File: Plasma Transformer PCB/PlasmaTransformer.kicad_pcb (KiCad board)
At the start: 2 copper layers, 90 x 90 mm, 92 parts, among them J1 Barrel_Jack_MountingPin, J10 Conn_01x01_Socket, J11 Screw_Terminal_01x01, J12 Screw_Terminal_01x01, J13 Conn_01x01_Socket, J14 Conn_01x01_Socket, J15 Conn_01x01_Socket, J16 Conn_01x01_Socket, J17 Conn_01x01_Socket, J18 Conn_01x01_Socket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

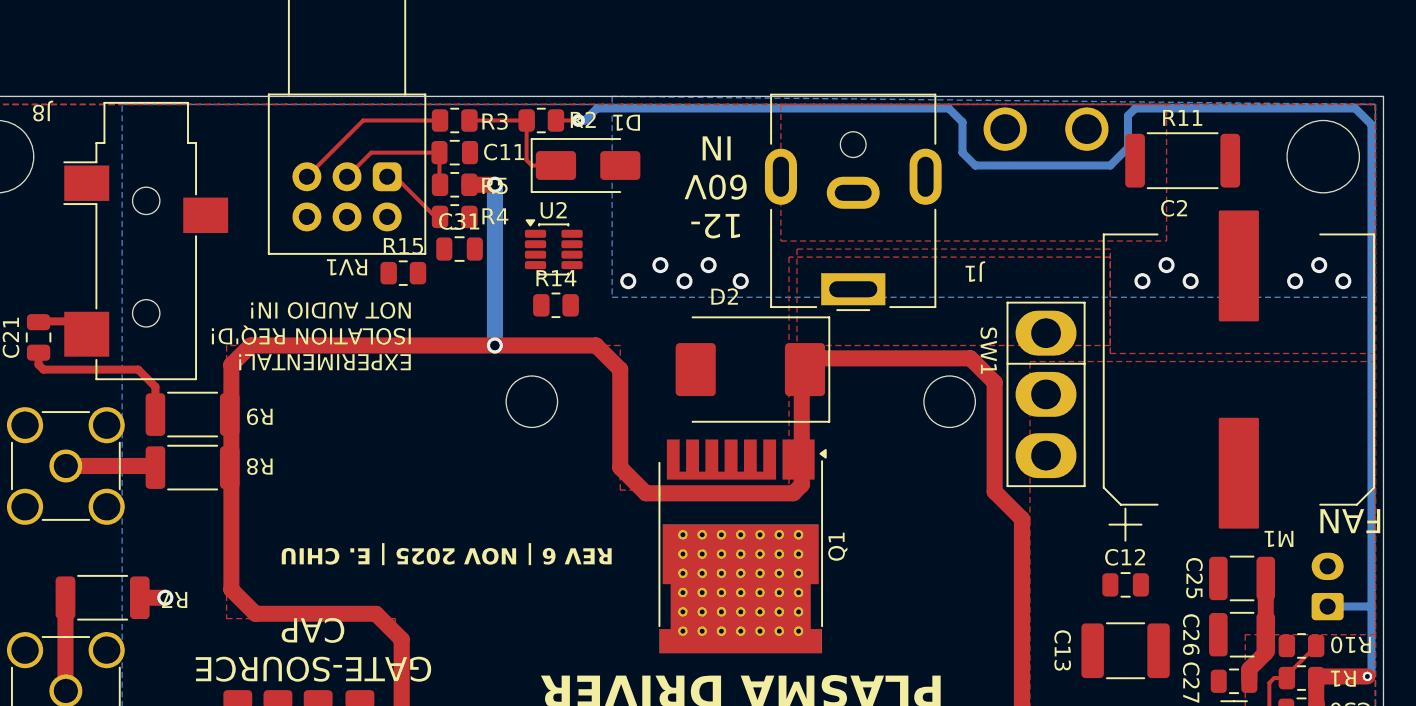
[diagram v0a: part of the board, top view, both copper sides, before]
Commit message: layout of feedback circuit
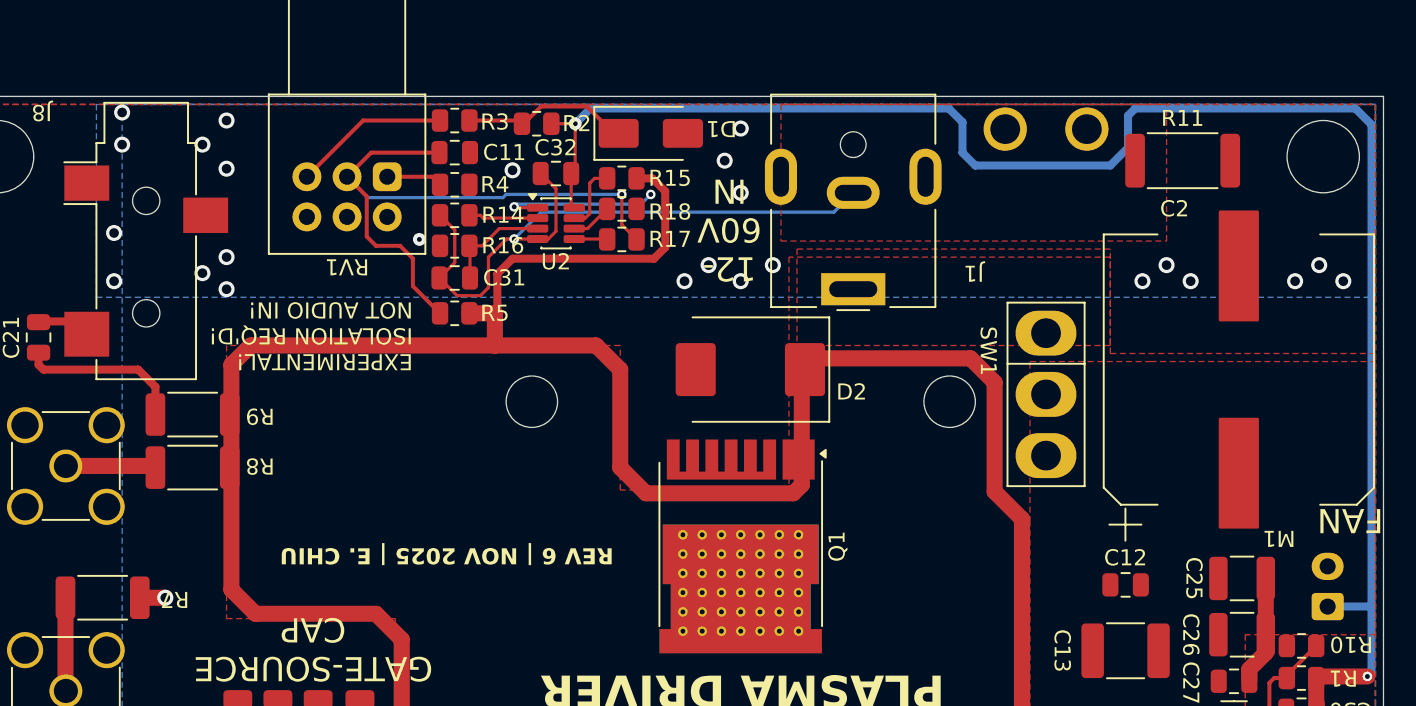
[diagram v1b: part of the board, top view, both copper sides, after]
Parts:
- added C32: 1nF, Capacitor_SMD:C_0805_2012Metric, F.Cu at (93.5, 59.8)
- added R16: 1k, Resistor_SMD:R_0805_2012Metric, F.Cu at (87.2, 64.3)
- added R17: 1k, Resistor_SMD:R_0805_2012Metric, F.Cu at (97.6, 63.9)
- added R18: 1k, Resistor_SMD:R_0805_2012Metric, F.Cu at (97.6, 62.0)
- U2: value LM358 -> TLV9302IDDFR
- moved R15 14.8 mm to (97.6, 60.1)
- moved R14 8.43 mm to (87.2, 62.4)
- moved R5 8.00 mm to (87.2, 68.5)
- moved D1 4.38 mm to (99.4, 57.3)
- moved R4 2.00 mm to (87.2, 60.5)
- moved C31 1.82 mm to (87.2, 66.3)
- moved U2 1.63 mm to (93.5, 62.9)
- moved R2 0.35 mm to (92.3, 56.7)
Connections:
- C31 pad 1: GND -> /GND-IN
- R14 pad 2: Net-(U2A-+) -> Net-(U2A--)
- U2 pad 1: Net-(U2B--) -> Net-(R12-Pad2)
- U2 pad 2: GND -> Net-(U2A--)
- U2 pad 4: GND -> /GND-IN
- U2 pad 5: unconnected-(U2B-+-Pad5) -> Net-(U2B-+)
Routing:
- net /GND-IN: track 0.00 -> 41.4 mm, vias 0 -> 1
- net Net-(C11-Pad2): track 8.39 -> 39.0 mm, vias 0 -> 1
- net /GATE: track 150.9 -> 162.1 mm, vias 2 -> 0
- net Net-(R12-Pad2): track 0.00 -> 10.3 mm, vias 0 -> 2
- net Net-(U2A-+): track 0.00 -> 6.71 mm
- net +12V: track 107.3 -> 112.8 mm
- net Net-(U2A--): track 0.00 -> 4.32 mm
- net Net-(R15-Pad1): track 0.00 -> 4.19 mm
- net Net-(U2B--): track 0.00 -> 2.56 mm
- net /REF10V: track 8.00 -> 10.4 mm
- net Net-(U2B-+): track 0.00 -> 2.06 mm
- net Net-(R4-Pad1): track 4.32 -> 3.78 mm
- net GND: vias 12 -> 26

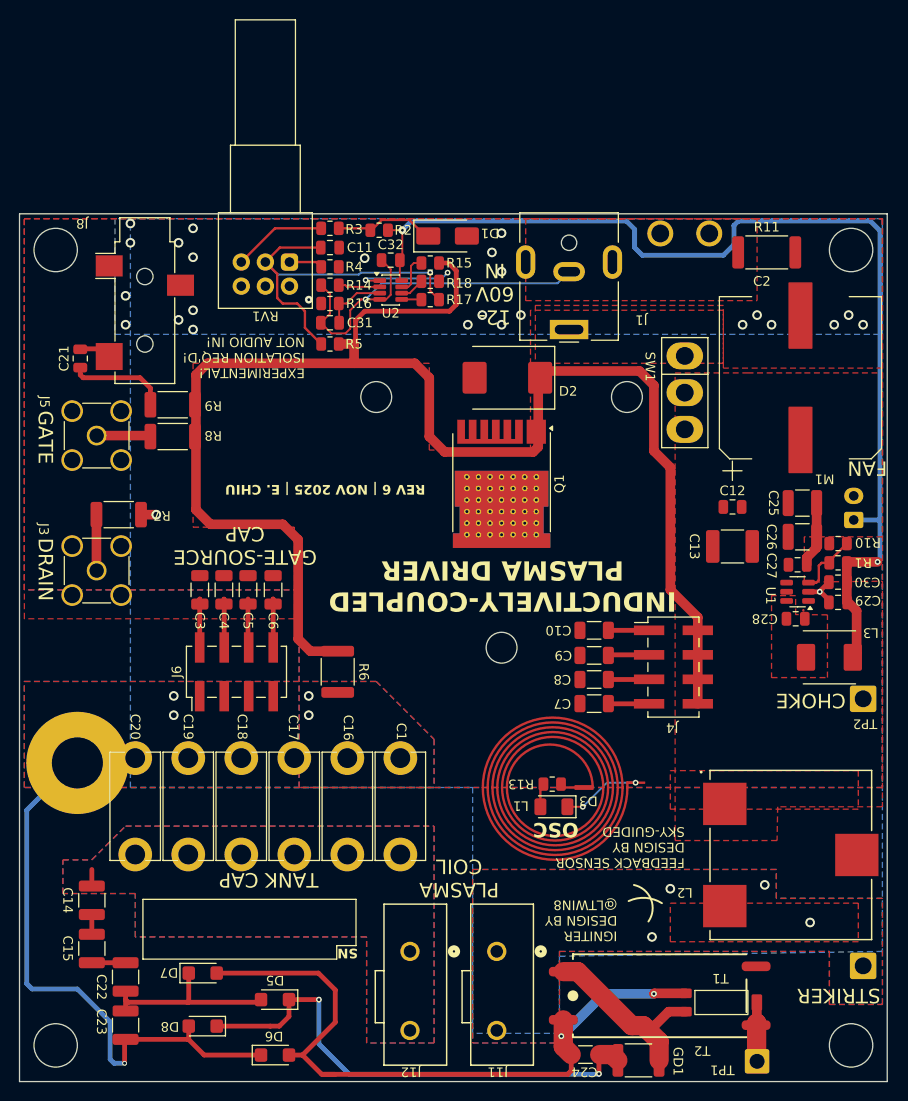
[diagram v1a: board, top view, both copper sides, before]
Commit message: routing complete, DRC check OK
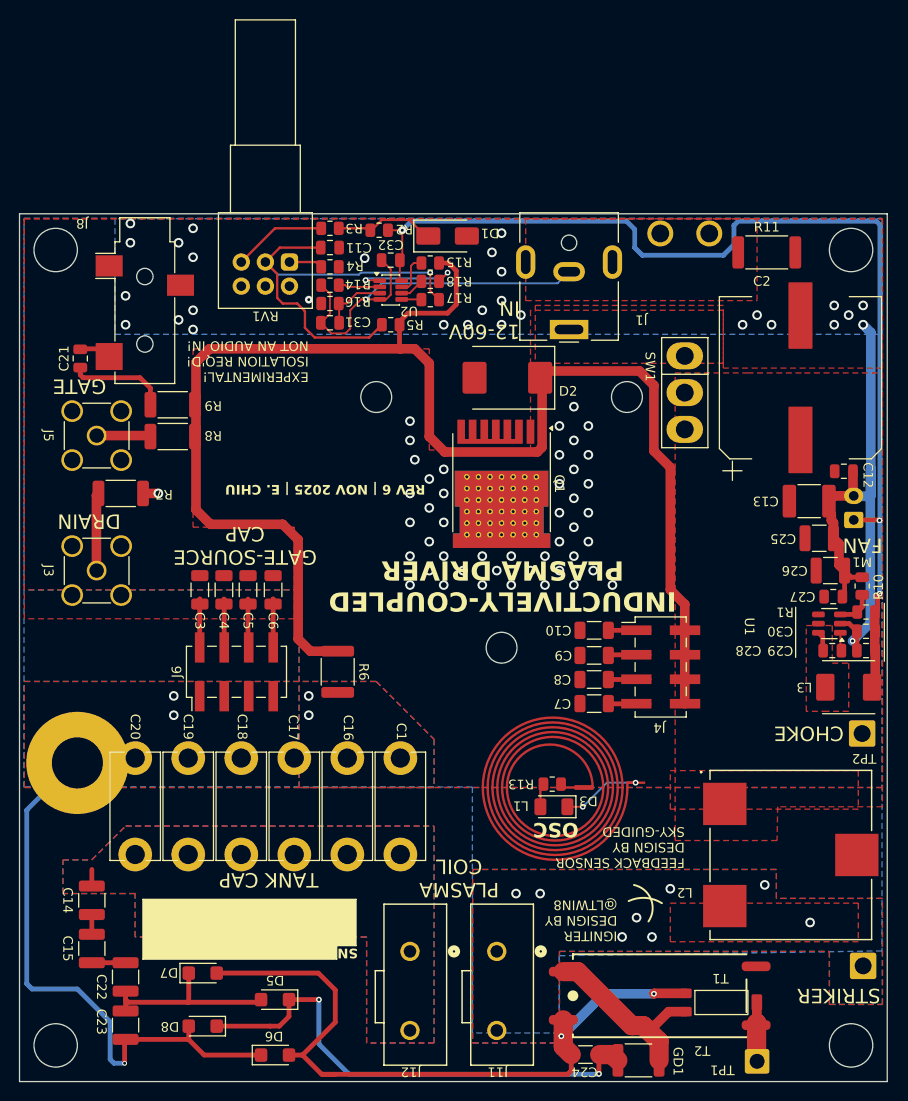
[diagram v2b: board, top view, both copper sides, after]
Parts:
- moved C12 12.1 mm to (140.5, 81.7), turned to 180 degrees
- moved C13 9.24 mm to (136.9, 84.8), turned to 180 degrees
- moved R5 6.61 mm to (93.5, 66.5)
- moved C30 5.87 mm to (142.8, 98.3)
- moved R1 5.87 mm to (142.8, 96.3)
- moved C29 5.78 mm to (142.8, 100.3)
- moved R10 5.06 mm to (142.4, 93.6), turned to 90 degrees
- moved C28 5.03 mm to (139.3, 100.3)
- moved C27 4.96 mm to (139.4, 94.7)
- moved U1 4.67 mm to (139.0, 97.5)
- moved C26 4.55 mm to (139.1, 92.0)
- moved C25 4.05 mm to (137.9, 88.7)
- moved L3 3.69 mm to (141.0, 104.1)
- moved TP2 3.60 mm to (142.4, 108.9)
- moved R7 2.21 mm to (65.5, 84.0)
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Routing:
- net GND: track 10.7 -> 63.6 mm, vias 26 -> 30
- net Net-(C11-Pad2): track 39.0 -> 45.6 mm
- net /GATE: track 162.1 -> 157.4 mm
- net Net-(U1-FB): track 6.63 -> 3.97 mm
- net Net-(J3-In): track 5.81 -> 8.10 mm
- net /12VSW: track 0.00 -> 2.05 mm
- net Net-(R12-Pad2): track 10.3 -> 11.6 mm
- net Net-(U1-CB): track 0.73 -> 1.90 mm
- net +12V: track 112.8 -> 113.0 mm, vias 2 -> 3
- net /DRAIN: vias 5 -> 54
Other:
- board text added: "12-60V IN"
- board text added: "EXPERIMENTAL! ISOLATION REQ'D! NOT AN AUDIO IN!"
- board text removed: "12- 60V IN"
- board text removed: "EXPERIMENTAL! ISOLATION REQ'D! NOT AUDIO IN!"

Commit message: add QR code for docs to backside silkscreen
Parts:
- added G***: LOGO, ALibrary:PlasmaTransformer-GitHub-QR-silk, B.Cu at (127.5, 133.5)
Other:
- board text added: "Plasma Transformer Documentation on GitHub Parts list, 3D prints, instructions, debugging"

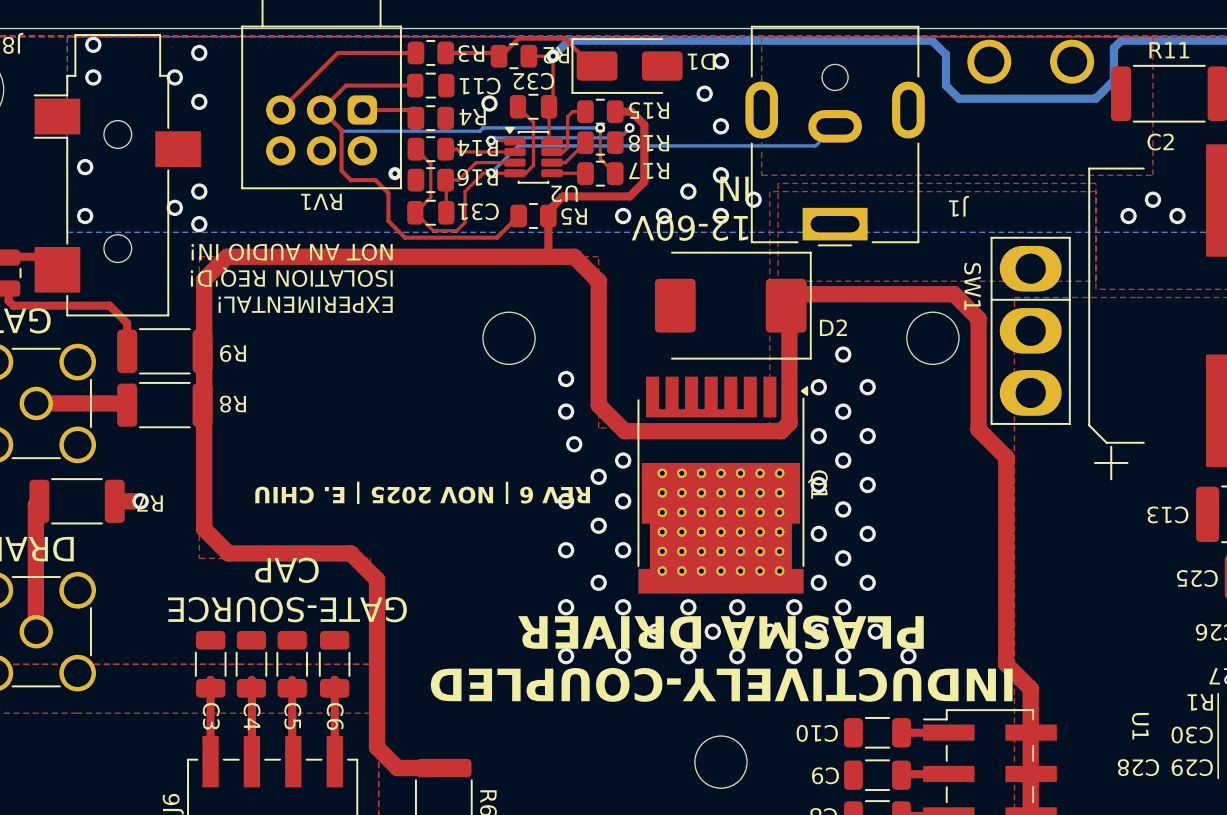
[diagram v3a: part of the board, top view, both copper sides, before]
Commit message: update silkscreens
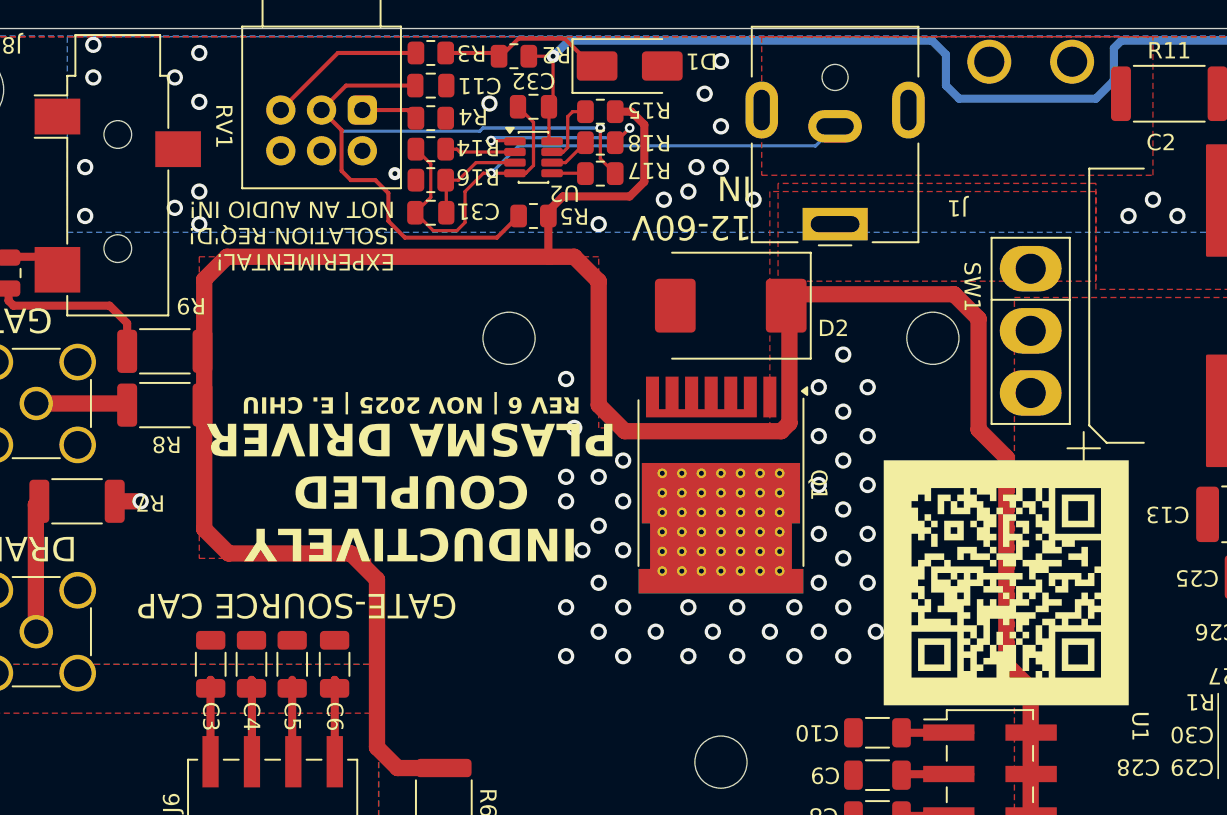
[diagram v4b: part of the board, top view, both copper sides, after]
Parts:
- added G***: LOGO, ALibrary:PlasmaTransformer-GitHub-QR-silk, F.Cu at (122.5, 89.0)
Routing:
- net /DRAIN: vias 54 -> 53
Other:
- board text added: "INDUCTIVELY COUPLED PLASMA DRIVER"
- board text removed: "INDUCTIVELY-COUPLED PLASMA DRIVER"

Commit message: generate manufacturing files
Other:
- board text added: "FAB NOTES: 1. FINISH: HASL LEAD FREE, ALTERNATE ENIG OK 2. SOLDERMASK: BLACK 3. SILKSCREEN: WHITE 4. LAYERS: 2 5. TOP AND BOTTOM WEIGHT: 1OZ 6. INNER LAYERS WEIGHT: 1OZ 7. TRACE/SPACE: 6MIL/6MIL 8. MINIMUM DRILL: 0.3MM 9. FINISHED THICKNESS: 1.6MM 10: CONTROLLED IMPEDANCE: NO 11. ITAR: NO 12. BOARD DIMENSIONS: 90MM x 90MM ASSY NOTES: 1. CLASS 2 ASSEMBLY 2. LEAD-FREE SOLDER 3. DO NOT POPULATE REFE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"
- board text added: "GATE-DRAIN CAP"
- board text removed: "FAB NOTES: 1. FINISH: HASL LEAD FREE, ALTERNATE ENIG OK 2. SOLDERMASK: WHITE 3. SILKSCREEN: BLACK 4. LAYERS: 2 5. TOP AND BOTTOM WEIGHT: 1OZ 6. INNER LAYERS WEIGHT: 1OZ 7. TRACE/SPACE: 6MIL/6MIL 8. MINIMUM DRILL: 0.3MM 9. FINISHED THICKNESS: 1.6MM 10: CONTROLLED IMPEDANCE: NO 11. ITAR: NO 12. BOARD DIMENSIONS: 90MM x 90MM ASSY NOTES: 1. CLASS 2 ASSEMBLY 2. LEAD-FREE SOLDER 3. DO NOT POPULATE REFE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"
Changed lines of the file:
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@@
 		(tenting front back)
 		(pcbplotparams
-			(layerselection 0x00000000_00000000_55555f55_575775ff)
+			(layerselection 0x00000000_00000000_55555f5d_575775ff)
 			(plot_on_all_layers_selection 0x00000000_00000000_00000000_00000000)
 			(disableapertmacros no)
@@
 		(tags "resistor")
 		(property "Reference" "R11"
-			(at 0 -2.63 0)
+			(at 0 -2.7 180)
 			(unlocked yes)
 			(layer "F.SilkS")
@@
 		(tags "Diode SMC (DO-214AB)")
 		(property "Reference" "D2"
-			(at -6.3 -1.4 0)
+			(at -6.3 -1.2 180)
 			(unlocked yes)
 			(layer "F.SilkS")
@@
 		(tags "Surface mounted pin header SMD 2x04 2.54mm double row")
 		(property "Reference" "J4"
-			(at -0.125 6.29 180)
+			(at 5.7 3.9 180)
 			(unlocked yes)
 			(layer "F.SilkS")
@@
 		(tags "capacitor electrolytic")
 		(property "Reference" "C2"
-			(at 10 -4 0)
+			(at 9.4 -7.6 180)
 			(unlocked yes)
 			(layer "F.SilkS")
@@
 		(tags "resistor")
 		(property "Reference" "R10"
-			(at -0.1 1.7 90)
+			(at 0.3 1.6 270)
 			(unlocked yes)
 			(layer "F.SilkS")
@@
 		(layer "User.2")
 	)
+	(gr_rect
+		(start 59.4 88.6)
+		(end 66.4 96)
+		(stroke
+			(width 0.1)
+			(type solid)
+		)
+		(fill yes)
+		(layer "User.2")
+	)
 	(gr_circle
 		(center 60.9 111.8)
@@
 	)
 	(gr_rect
-		(start 77.25 32.4)
-		(end 89.75 54.9)
+		(start 74.15 33.15)
+		(end 86.65 55.65)
 		(stroke
 			(width 0.1)
@@
 	)
 	(gr_rect
-		(start 174.5 121.5)
-		(end 181.5 133.5)
+		(start 118.1 95.9)
+		(end 125.1 107.9)
 		(stroke
 			(width 0.1)
@@
 		(layer "User.2")
 	)
+	(gr_rect
+		(start 59.7 73.75)
+		(end 66.7 81.45)
+		(stroke
+			(width 0.1)
+			(type solid)
+		)
+		(fill yes)
+		(layer "User.2")
+	)
 	(gr_circle
 		(center 83.497056 121.5)
@@
 	)
 	(gr_rect
-		(start 130.25 41)
-		(end 142.75 46.5)
+		(start 105.85 51.8)
+		(end 118.35 57.3)
 		(stroke
 			(width 0.1)
@@
 		(layer "User.3")
 	)
+	(gr_rect
+		(start 82.334418 63.834418)
+		(end 131.795172 108.6)
+		(stroke
+			(width 0.1)
+			(type solid)
+		)
+		(fill yes)
+		(layer "User.3")
+	)
 	(gr_text "EXPERIMENTAL!\nISOLATION REQ'D!\nNOT AN AUDIO IN!"
 		(at 85 65.5 180)
@@
 		)
 	)
+	(gr_text "GATE-DRAIN CAP"
+		(at 116.8 107.8 180)
+		(layer "F.SilkS")
+		(effects
+			(font
+				(size 1.5 1.5)
+				(thickness 0.25)
+			)
+			(justify bottom)
+		)
+	)
 	(gr_text "REV 6 | NOV 2025 | E. CHIU"
 		(at 86 77.5 180)
@@
 		)
 	)
-	(gr_text "FAB NOTES:\n1. FINISH: HASL LEAD FREE, ALTERNATE ENIG OK\n2. SOLDERMASK: WHITE\n3. SILKSCREEN: BLACK\n4. LAYERS: 2\n5. TOP AND BOTTOM WEIGHT: 1OZ\n6. INNER LAYERS WEIGHT: 1OZ\n7. TRACE/SPACE: 6MIL/6MIL\n8. MINIMUM DRILL: 0.3MM\n9. FINISHED THICKNESS: 1.6MM\n10: CONTROLLED IMPEDANCE: NO\n11. ITAR: NO\n12. BOARD DIMENSIONS: 90MM x 90MM\n\nASSY NOTES:\n1. CLASS 2 ASSEMBLY\n2. LEAD-FREE SOLDER\n3. DO NOT POPULATE REFERENCE DESIGNATORS THAT ARE MARKED IN THE BOM AS DNP.\n4. J7, J9, J10, J13-J21 ARE PRESS-FIT.  DO NOT SOLDER.\n5. POLARITY MARKERS\n    - PIN 1 IS MARKED BY A DOT, TRIANGLE, BEVEL, OR SQUARE PTH PAD\n    - POSITIVE TERMINAL FOR POLARIZED CAPACITORS IS INDICATED BY A '+' SYMBOL\n    - CATHODE TERMINAL FOR DIODES AND LEDS IS INDICATED BY A CLOSED SILKSCREEN END\n6. IF OUTDOOR USE IS REQUIRED, CONFORMAL COAT ACRYLIC CA3002 OR EQUIVALENT, AFTER Q1 AND STRIKER WIRE ARE INSTALLED.\n   MASK AREAS INDICATED BY COLOR AREAS ON LAYERS F.CCmask and B.CCmask"
+	(gr_text "FAB NOTES:\n1. FINISH: HASL LEAD FREE, ALTERNATE ENIG OK\n2. SOLDERMASK: BLACK\n3. SILKSCREEN: WHITE\n4. LAYERS: 2\n5. TOP AND BOTTOM WEIGHT: 1OZ\n6. INNER LAYERS WEIGHT: 1OZ\n7. TRACE/SPACE: 6MIL/6MIL\n8. MINIMUM DRILL: 0.3MM\n9. FINISHED THICKNESS: 1.6MM\n10: CONTROLLED IMPEDANCE: NO\n11. ITAR: NO\n12. BOARD DIMENSIONS: 90MM x 90MM\n\nASSY NOTES:\n1. CLASS 2 ASSEMBLY\n2. LEAD-FREE SOLDER\n3. DO NOT POPULATE REFERENCE DESIGNATORS THAT ARE MARKED IN THE BOM AS DNP.\n4. J7, J9, J10, J13-J21 ARE PRESS-FIT.  DO NOT SOLDER.\n5. POLARITY MARKERS\n    - PIN 1 IS MARKED BY A DOT, TRIANGLE, BEVEL, OR SQUARE PTH PAD\n    - POSITIVE TERMINAL FOR POLARIZED CAPACITORS IS INDICATED BY A '+' SYMBOL\n    - CATHODE TERMINAL FOR DIODES AND LEDS IS INDICATED BY A CLOSED SILKSCREEN END\n6. IF OUTDOOR USE IS REQUIRED, CONFORMAL COAT ACRYLIC CA3002 OR EQUIVALENT, AFTER Q1 AND STRIKER WIRE ARE INSTALLED.\n   MASK AREAS INDICATED BY COLOR AREAS ON LAYERS F.CCmask and B.CCmask"
 		(at 162.4 77.6 0)
 		(layer "F.Fab")
